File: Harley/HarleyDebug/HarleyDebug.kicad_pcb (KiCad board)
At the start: 2 copper layers, 30.8 x 22 mm, 10 parts, among them P1 CONN_02X05, P2 CONN_02X07, P3 CONN_01X03, P4 CONN_01X04

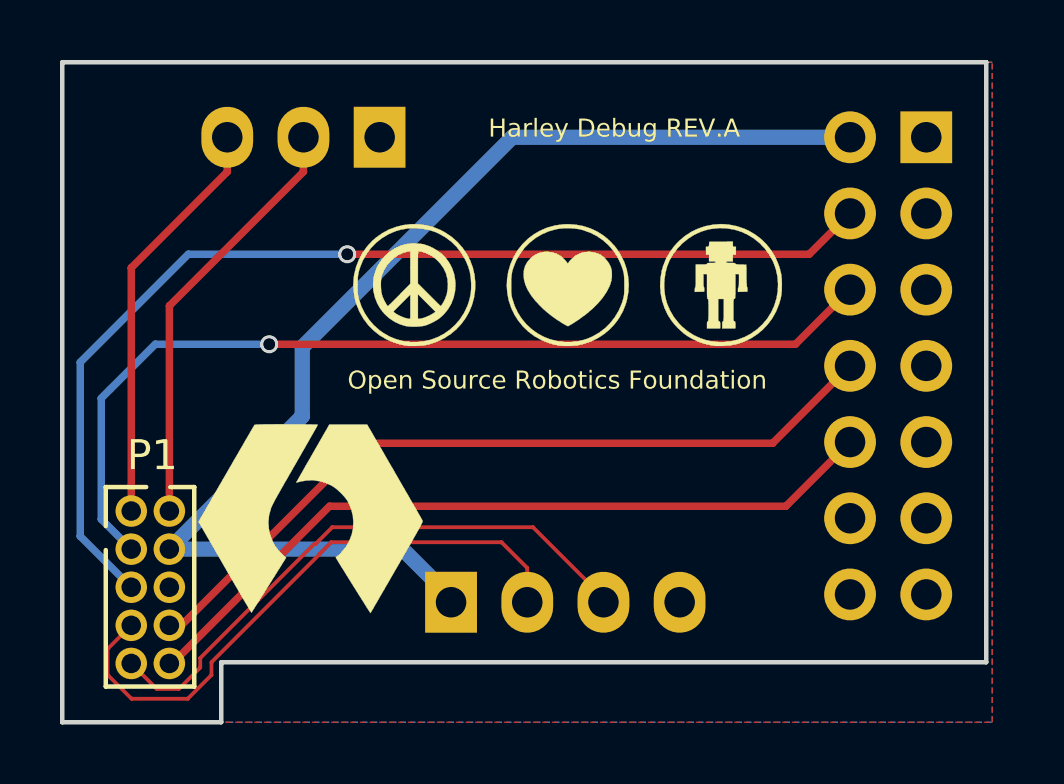
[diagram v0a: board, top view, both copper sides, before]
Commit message: minor trace reroute and silkscreen improvements
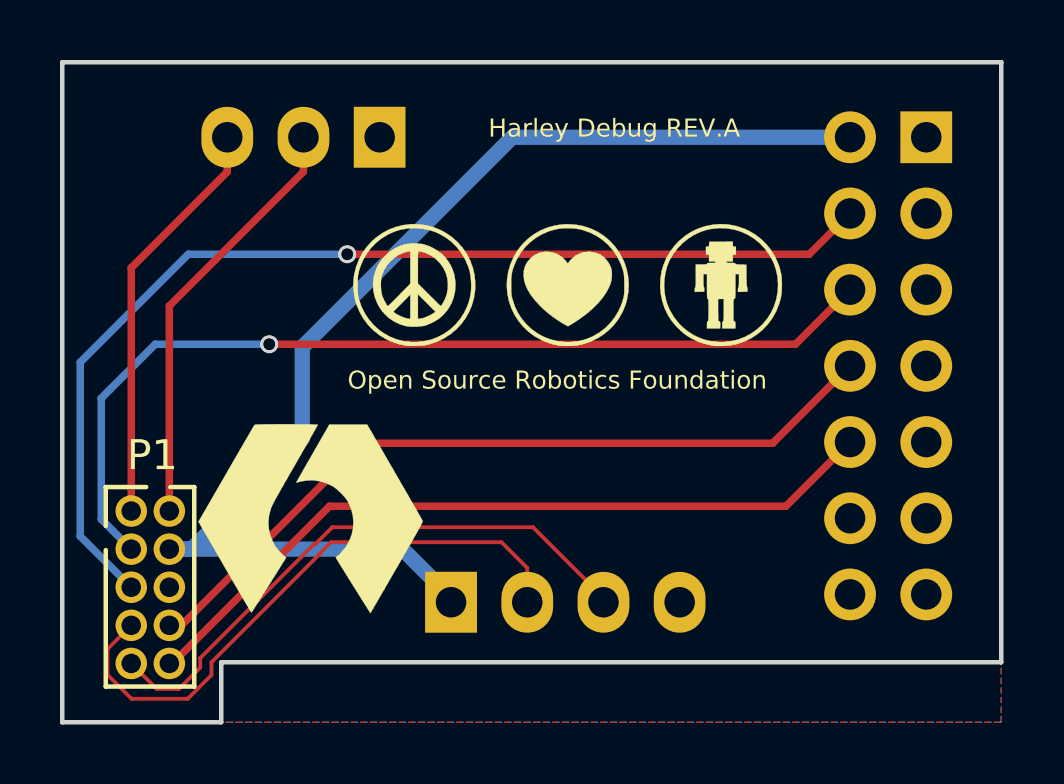
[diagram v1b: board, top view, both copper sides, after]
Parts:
- removed the G*** at (42.1, 195.0)
- removed the G*** at (42.1, 176.8)
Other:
- board size 30.8 x 22 mm -> 31.3 x 22 mm
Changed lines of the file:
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@@
 (kicad_pcb (version 4) (host pcbnew 0.201603210401+6634~43~ubuntu14.04.1-product)
   (general
-    (links 0)
+    (links 19)
     (no_connects 0)
-    (area 11.924999 175.924999 42.875001 198.075001)
+    (area 11.924999 175.924999 43.375001 198.075001)
     (thickness 1.6)
-    (drawings 20)
-    (tracks 62)
+    (drawings 25)
+    (tracks 63)
     (zones 0)
-    (modules 10)
+    (modules 8)
     (nets 13)
   )
@@
     (uvia_dia 0.3)
     (uvia_drill 0.1)
-  )
-  (module silkscreen:GND (layer B.Cu)
-    (at 42.1 195 180)
-    (fp_text reference G*** (at 0 0 180) (layer B.SilkS) hide
-      (effects (font (thickness 0.3)) (justify mirror))
-    )
-    (fp_text value LOGO (at 0.75 0 180) (layer B.SilkS) hide
-      (effects (font (thickness 0.3)) (justify mirror))
-    )
-    (fp_poly (pts (xy 0.135467 -0.630767) (xy 0 -0.630767) (xy -0.135466 -0.630767) (xy -0.135466 -0.605367)
-      (xy -0.135466 -0.579967) (xy 0 -0.579967) (xy 0.135467 -0.579967) (xy 0.135467 -0.605367)
-      (xy 0.135467 -0.630767) (xy 0.135467 -0.630767)) (layer B.SilkS) (width 0.1))
-    (fp_poly (pts (xy 0.287867 -0.359833) (xy 0 -0.359833) (xy -0.287866 -0.359833) (xy -0.287866 -0.334433)
-      (xy -0.287866 -0.309033) (xy 0 -0.309033) (xy 0.287867 -0.309033) (xy 0.287867 -0.334433)
-      (xy 0.287867 -0.359833) (xy 0.287867 -0.359833)) (layer B.SilkS) (width 0.1))
-    (fp_poly (pts (xy 0.461434 -0.093133) (xy 0 -0.093133) (xy -0.461433 -0.093133) (xy -0.461433 -0.067733)
-      (xy -0.461433 -0.042333) (xy -0.243416 -0.042333) (xy -0.0254 -0.042333) (xy -0.0254 0.281517)
-      (xy -0.0254 0.605367) (xy 0 0.605367) (xy 0.0254 0.605367) (xy 0.0254 0.281517)
-      (xy 0.0254 -0.042333) (xy 0.243417 -0.042333) (xy 0.461434 -0.042333) (xy 0.461434 -0.067733)
-      (xy 0.461434 -0.093133) (xy 0.461434 -0.093133)) (layer B.SilkS) (width 0.1))
-  )
-  (module silkscreen:GND (layer B.Cu)
-    (at 42.1 176.8 180)
-    (fp_text reference G*** (at 0 0 180) (layer B.SilkS) hide
-      (effects (font (thickness 0.3)) (justify mirror))
-    )
-    (fp_text value LOGO (at 0.75 0 180) (layer B.SilkS) hide
-      (effects (font (thickness 0.3)) (justify mirror))
-    )
-    (fp_poly (pts (xy 0.135467 -0.630767) (xy 0 -0.630767) (xy -0.135466 -0.630767) (xy -0.135466 -0.605367)
-      (xy -0.135466 -0.579967) (xy 0 -0.579967) (xy 0.135467 -0.579967) (xy 0.135467 -0.605367)
-      (xy 0.135467 -0.630767) (xy 0.135467 -0.630767)) (layer B.SilkS) (width 0.1))
-    (fp_poly (pts (xy 0.287867 -0.359833) (xy 0 -0.359833) (xy -0.287866 -0.359833) (xy -0.287866 -0.334433)
-      (xy -0.287866 -0.309033) (xy 0 -0.309033) (xy 0.287867 -0.309033) (xy 0.287867 -0.334433)
-      (xy 0.287867 -0.359833) (xy 0.287867 -0.359833)) (layer B.SilkS) (width 0.1))
-    (fp_poly (pts (xy 0.461434 -0.093133) (xy 0 -0.093133) (xy -0.461433 -0.093133) (xy -0.461433 -0.067733)
-      (xy -0.461433 -0.042333) (xy -0.243416 -0.042333) (xy -0.0254 -0.042333) (xy -0.0254 0.281517)
-      (xy -0.0254 0.605367) (xy 0 0.605367) (xy 0.0254 0.605367) (xy 0.0254 0.281517)
-      (xy 0.0254 -0.042333) (xy 0.243417 -0.042333) (xy 0.461434 -0.042333) (xy 0.461434 -0.067733)
-      (xy 0.461434 -0.093133) (xy 0.461434 -0.093133)) (layer B.SilkS) (width 0.1))
   )
   (module Pin_Headers:Pin_Header_Straight_2x05_Pitch1.27mm (layer F.Cu)
@@
       (xy 4.306832 -0.072571) (xy 4.314066 -0.083453) (xy 4.316242 -0.111901) (xy 4.316242 -0.111901)) (layer B.SilkS) (width 0.1))
   )
+  (gr_line (start 42.8 186) (end 42.8 195) (layer B.SilkS) (width 0.2))
+  (gr_line (start 43.2 186) (end 42.8 186) (layer B.SilkS) (width 0.2))
+  (gr_line (start 43.2 184) (end 43.2 186) (layer B.SilkS) (width 0.2))
+  (gr_line (start 42.8 184) (end 43.2 184) (layer B.SilkS) (width 0.2))
+  (gr_line (start 42.8 176.8) (end 42.8 184) (layer B.SilkS) (width 0.2))
   (gr_text "Harley Debug REV.A" (at 30.4 178.2) (layer F.SilkS)
     (effects (font (size 0.6 0.6) (thickness 0.13)))
@@
   (gr_line (start 17.3 198) (end 17.3 196) (layer Edge.Cuts) (width 0.15))
   (gr_line (start 12 198) (end 17.3 198) (layer Edge.Cuts) (width 0.15))
-  (gr_line (start 42.8 196) (end 42.8 176) (layer Edge.Cuts) (width 0.15))
+  (gr_line (start 43.3 196) (end 43.3 176) (layer Edge.Cuts) (width 0.15))
   (gr_line (start 12 176) (end 12 198) (layer Edge.Cuts) (width 0.15))
-  (gr_line (start 12 176) (end 42.8 176) (layer Edge.Cuts) (width 0.15))
-  (gr_line (start 17.3 196) (end 42.8 196) (layer Edge.Cuts) (width 0.15))
+  (gr_line (start 12 176) (end 43.3 176) (layer Edge.Cuts) (width 0.15))
+  (gr_line (start 17.3 196) (end 43.3 196) (layer Edge.Cuts) (width 0.15))
   (segment (start 14.3 190.96) (end 14.3 182.8524) (width 0.25) (layer F.Cu) (net 1))
   (segment (start 14.3 182.8524) (end 17.5 179.6524) (width 0.25) (layer F.Cu) (net 1))
@@
   (via (at 18.9 185.4) (size 0.6) (drill 0.4) (layers F.Cu B.Cu) (net 3))
   (segment (start 14.3 192.23) (end 13.934998 192.23) (width 0.25) (layer B.Cu) (net 3))
+  (segment (start 15.57 192.23) (end 16.312462 192.23) (width 0.508) (layer B.Cu) (net 4))
+  (segment (start 16.312462 192.23) (end 20 188.542462) (width 0.508) (layer B.Cu) (net 4))
+  (segment (start 20 188.542462) (end 20 185.5) (width 0.508) (layer B.Cu) (net 4))
+  (segment (start 20 185.5) (end 27 178.5) (width 0.508) (layer B.Cu) (net 4))
+  (segment (start 27 178.5) (end 38.26 178.5) (width 0.508) (layer B.Cu) (net 4))
   (segment (start 15.57 192.23) (end 23.3424 192.23) (width 0.508) (layer B.Cu) (net 4))
   (segment (start 23.3424 192.23) (end 24.96 193.8476) (width 0.508) (layer B.Cu) (net 4))
   (segment (start 24.96 193.8476) (end 24.96 194) (width 0.508) (layer B.Cu) (net 4))
-  (segment (start 20 185.5) (end 27 178.5) (width 0.508) (layer B.Cu) (net 4))
-  (segment (start 27 178.5) (end 38.26 178.5) (width 0.508) (layer B.Cu) (net 4))
-  (segment (start 20 187.8) (end 20 185.5) (width 0.508) (layer B.Cu) (net 4))
-  (segment (start 15.57 192.23) (end 20 187.8) (width 0.508) (layer B.Cu) (net 4))
   (segment (start 14.3 193.5) (end 12.6 191.8) (width 0.25) (layer B.Cu) (net 5))
   (segment (start 12.6 191.8) (end 12.6 186) (width 0.25) (layer B.Cu) (net 5))
@@
     (polygon
       (pts
-        (xy 12 176) (xy 12 198) (xy 17.5 198) (xy 43 198) (xy 43 176)
+        (xy 12 176) (xy 12 198) (xy 17.5 198) (xy 43.3 198) (xy 43.3 176)
       )
     )
@@
     (polygon
       (pts
-        (xy 12 176) (xy 12 198) (xy 43 198) (xy 43 176)
+        (xy 12 176) (xy 12 198) (xy 43.3 198) (xy 43.3 176)
       )
     )
